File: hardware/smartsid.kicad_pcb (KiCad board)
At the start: 2 copper layers, 50.8 x 57.8 mm, 63 parts, among them P1 INPUT, P2 CONTROL, P4 SOCKET LEFT, P5 OUTPUT, P6 SOCKET RIGHT, Q1 BC547, Q2 BC547, U1 GAL16V8, U2 SID2, U3 7812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

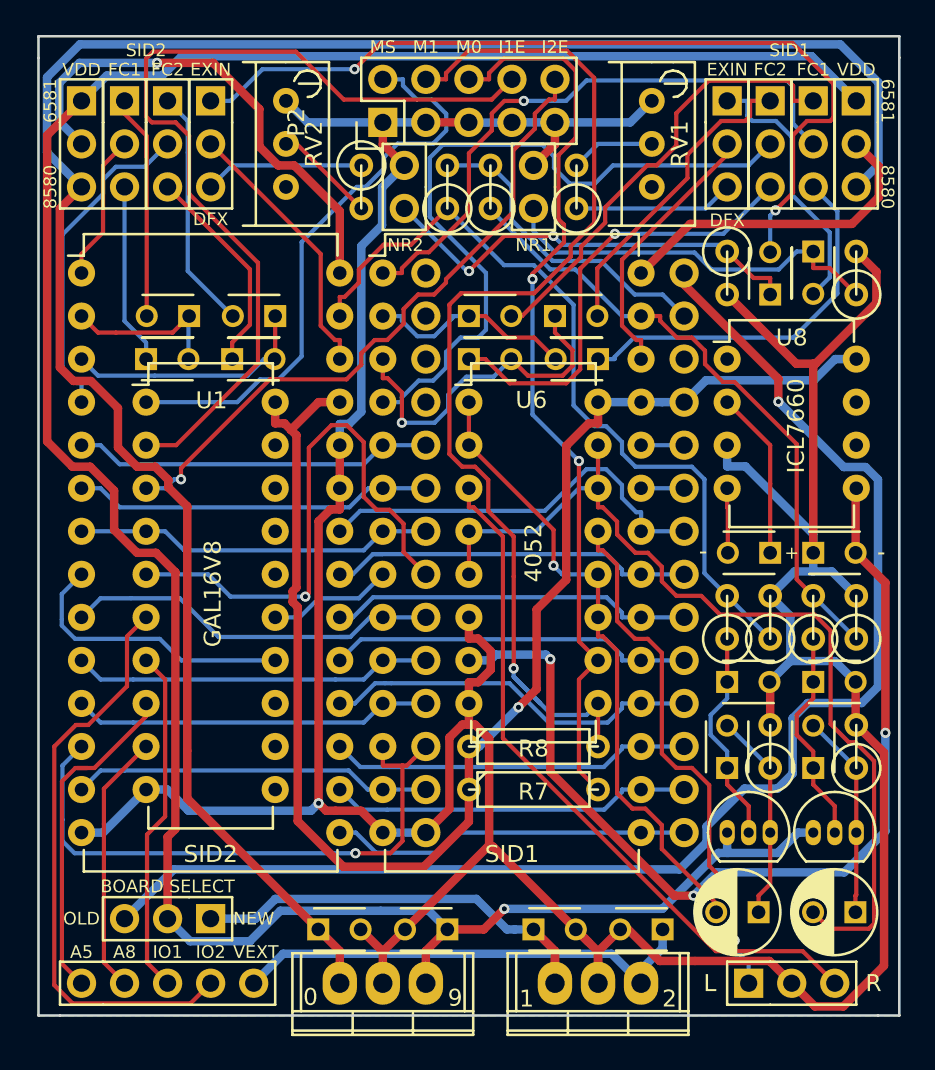
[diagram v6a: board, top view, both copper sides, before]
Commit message: Hardware: Improved routing, silkscreen
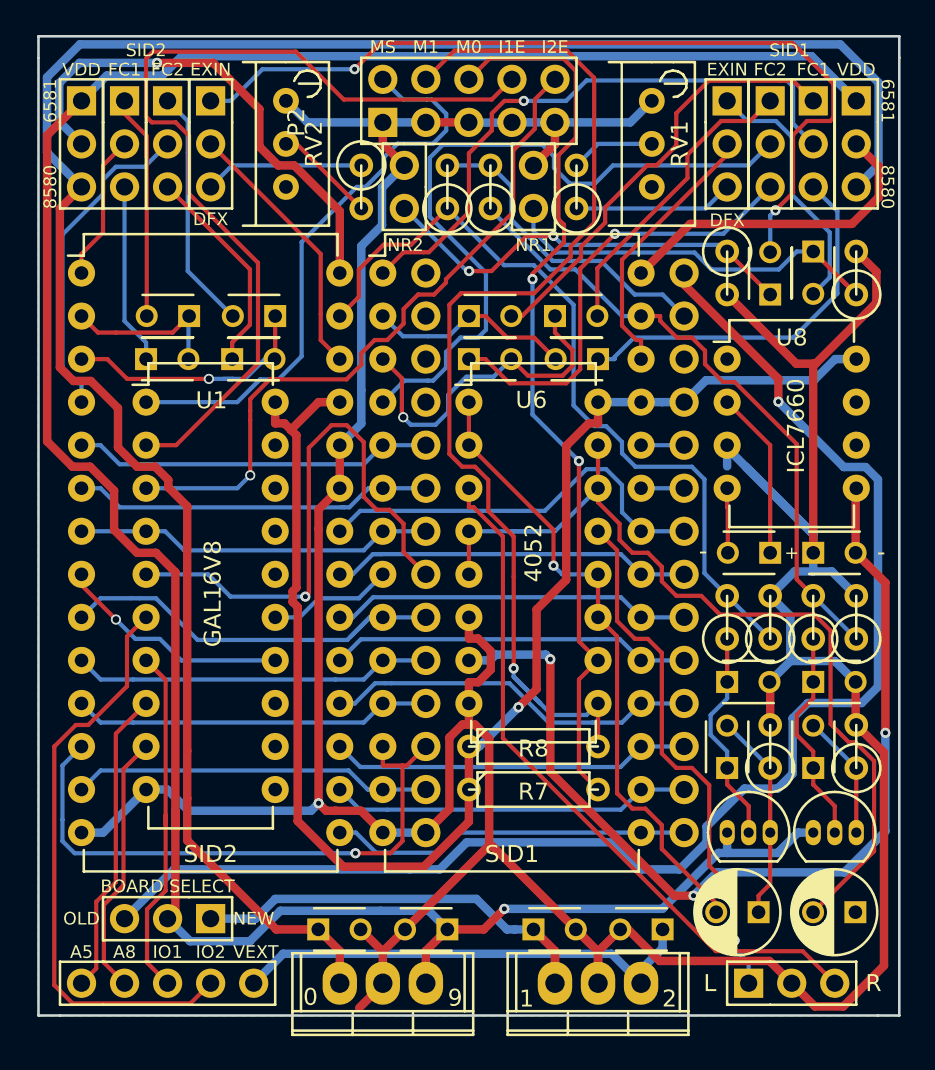
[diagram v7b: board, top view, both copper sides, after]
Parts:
- P2: footprint Pin_Headers:Pin_Header_Straight_2x05 -> Pinheaders:Pin_Header_Straight_2x05
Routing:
- net GND: track 235.7 -> 243.3 mm
- net Net-(C21-Pad2): track 12.1 -> 7.39 mm
- net /~CS2: track 17.0 -> 13.9 mm, vias 0 -> 1
- net /A5: track 20.3 -> 18.1 mm
- net /~IO1: track 20.5 -> 22.6 mm
- net /~IO2EN: track 38.9 -> 40.9 mm
- net /A0: track 22.7 -> 24.8 mm
- net /RIGHT: track 55.3 -> 53.2 mm
- net Net-(C14-Pad1): track 23.4 -> 25.0 mm
- net /+9V: track 120.4 -> 121.9 mm
- net VDD: track 82.5 -> 83.8 mm
- net /+12V: track 149.4 -> 150.4 mm
- net Net-(C1-Pad1): track 14.8 -> 15.5 mm, vias 0 -> 1
- net Net-(C13-Pad1): track 26.0 -> 25.4 mm
- net Net-(C11-Pad2): track 26.6 -> 26.1 mm
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
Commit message: Hardware: Improved routing, copper pours
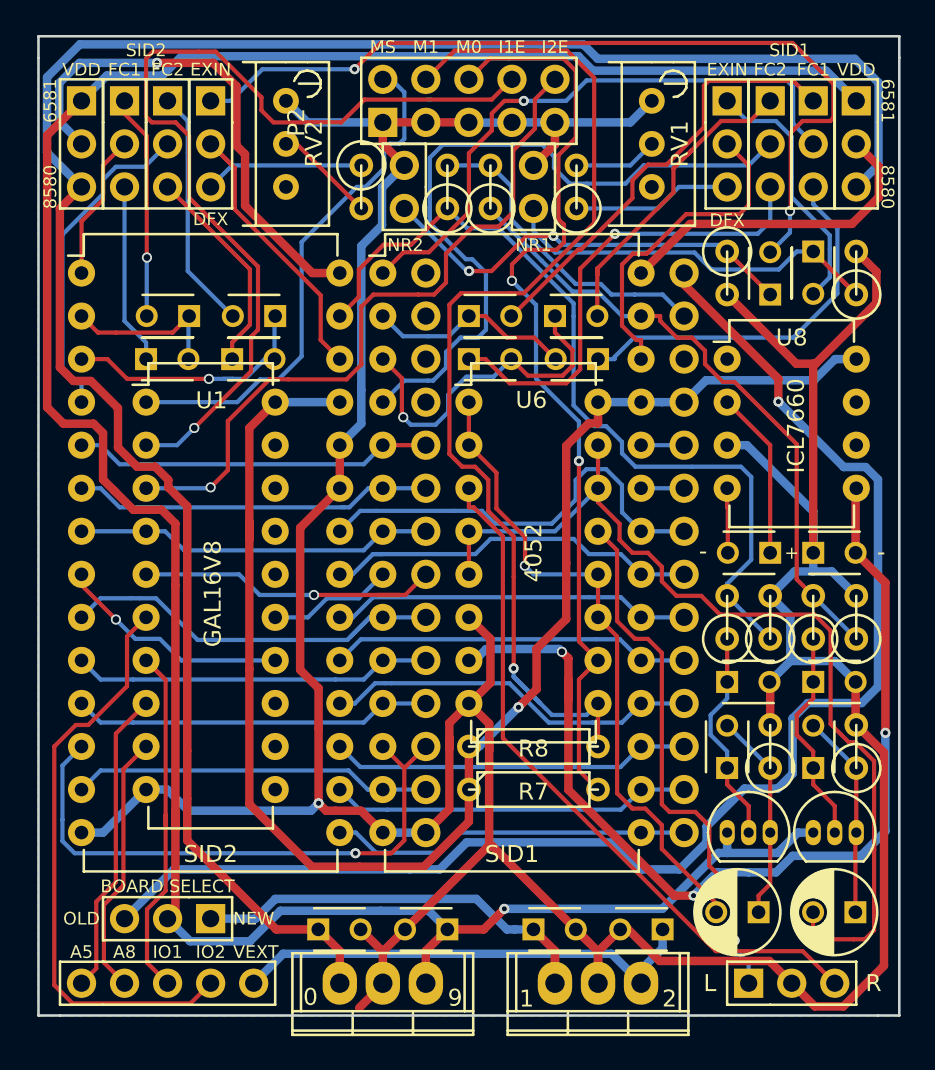
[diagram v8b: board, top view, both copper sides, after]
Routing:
- net /~CS: track 32.8 -> 19.1 mm
- net /RIGHT: track 53.2 -> 58.6 mm
- net Net-(C21-Pad2): track 7.39 -> 12.1 mm
- net /S1IN: track 15.9 -> 19.3 mm
- net /MS: track 34.3 -> 31.0 mm
- net VCC: track 86.5 -> 89.6 mm
- net /S2OUT: track 46.6 -> 49.5 mm
- net GND: track 243.3 -> 240.8 mm
- net /VEE: track 57.1 -> 59.2 mm
- net /M0: track 53.4 -> 55.4 mm
- net /S2IN: track 15.9 -> 17.9 mm
- net /~IO1EN: track 53.6 -> 55.2 mm, vias 0 -> 1
- net /D7: track 24.3 -> 25.6 mm
- net Net-(C10-Pad1): track 26.7 -> 27.8 mm
- net /~IO2EN: track 40.9 -> 42.0 mm
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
